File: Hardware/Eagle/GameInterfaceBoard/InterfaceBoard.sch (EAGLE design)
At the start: 22 parts

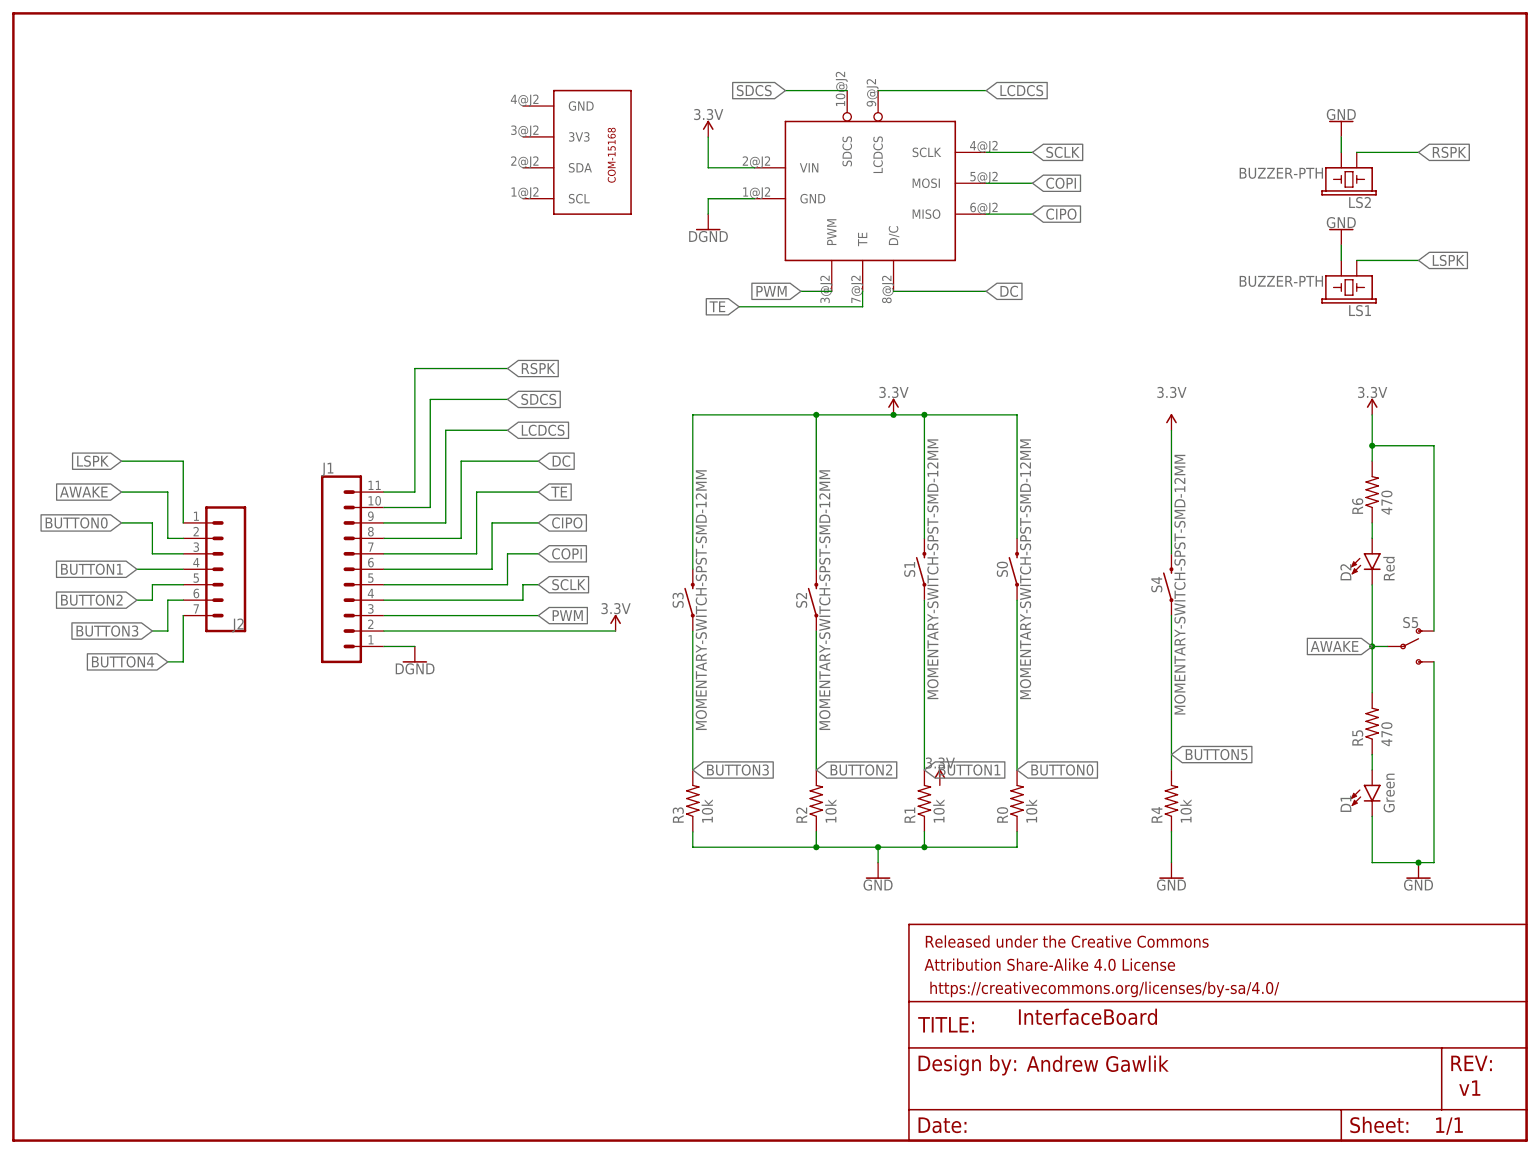
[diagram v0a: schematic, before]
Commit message: Added connection for button 4 and updated buttons to use through hole version and switched pins for easier connection on issue #2
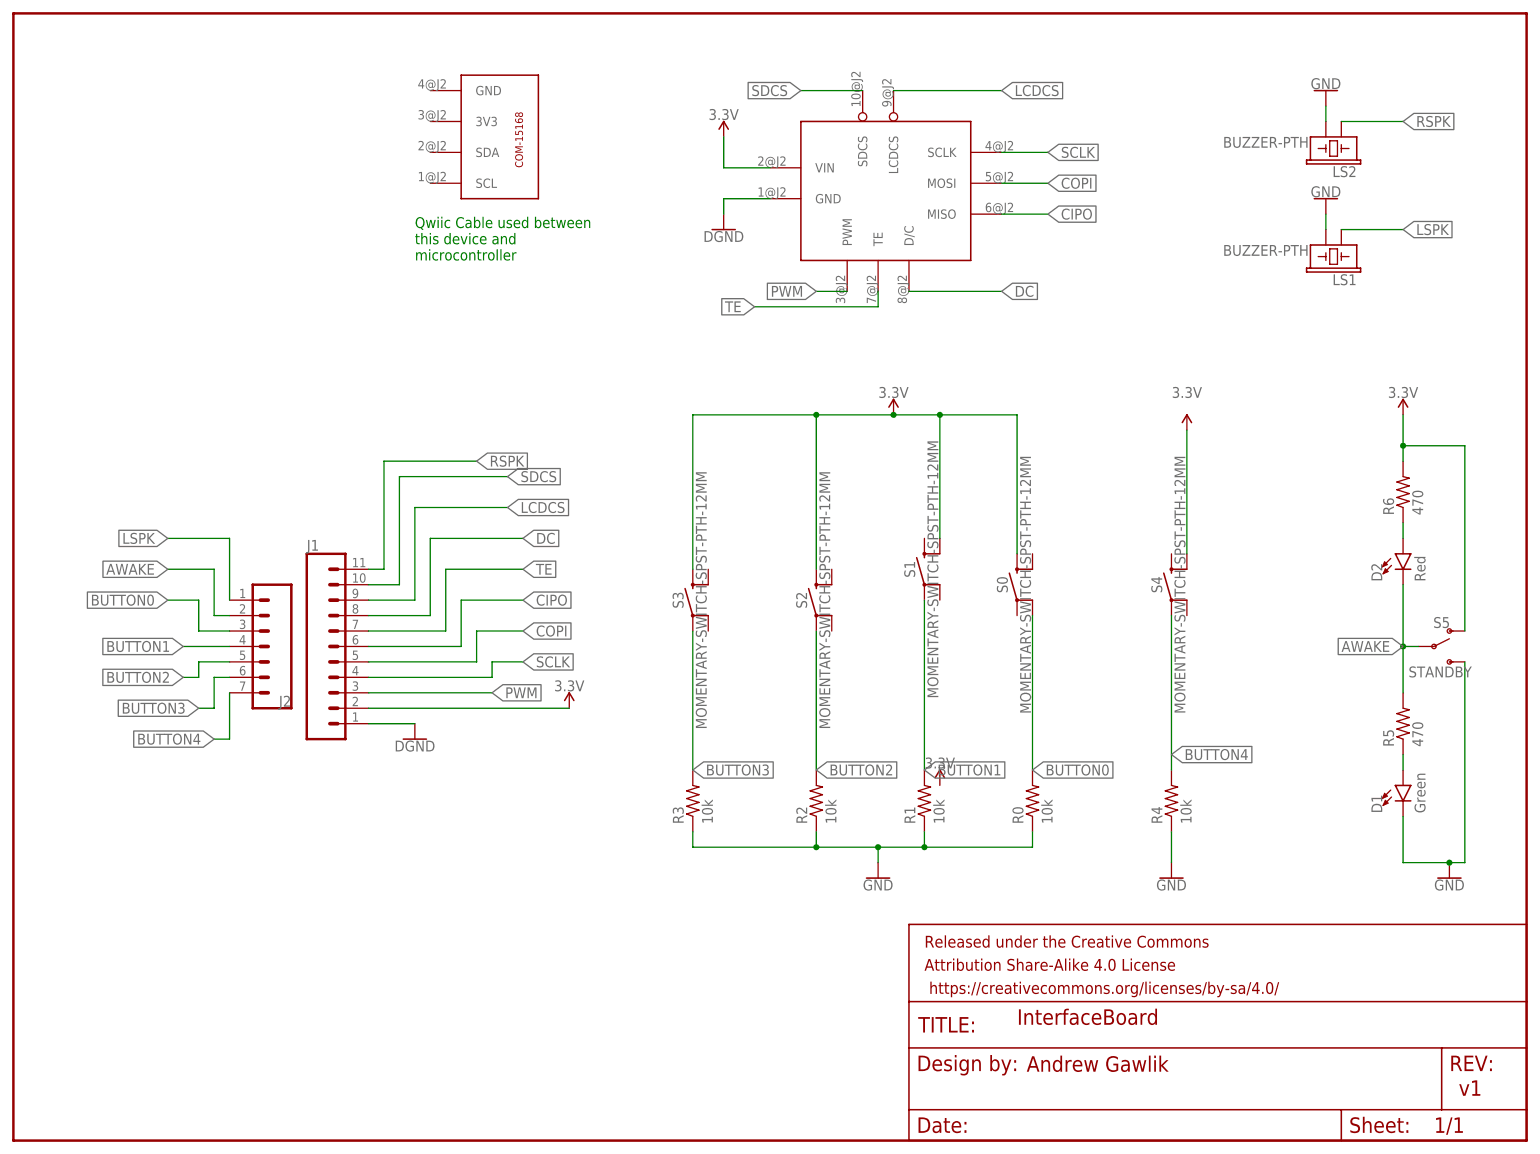
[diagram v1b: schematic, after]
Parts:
- removed A1: (no value), SparkFunBreakouts:LCD-15143
- removed U$1: COM-15168, SparkFunBreakouts:COM-15168
- added A2: TFT, SparkFunBreakouts:LCD-15143
- added A3: COM-15168, SparkFunBreakouts:COM-15168
- S0, S1, S2, S3, S4: value MOMENTARY-SWITCH-SPST-SMD-12MM -> MOMENTARY-SWITCH-SPST-PTH-12MM; device SparkFun-Switches:MOMENTARY-SWITCH-SPST-SMD-12MM -> SparkFun-Switches:MOMENTARY-SWITCH-SPST-PTH-12MM
- S5: value (none) -> STANDBY
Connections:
- removed net BUTTON5: R4.2, S4.1
- net 3.3V: now also A2.VIN, S0.3, S1.4, S2.3, S3.3, S4.4; no longer A1.VIN, S0.2, S1.2, S2.2, S3.2, S4.2
- net BUTTON0: now also S0.2; no longer S0.1
- net BUTTON4: now also R4.2, S4.1
- net CIPO: now also A2.MISO; no longer A1.MISO
- net COPI: now also A2.MOSI; no longer A1.MOSI
- net DC: now also A2.D/C; no longer A1.D/C
- net GND: now also A2.GND; no longer A1.GND
- net LCDCS: now also A2.LCDCS; no longer A1.LCDCS
- net PWM: now also A2.PWM; no longer A1.PWM
- net SCLK: now also A2.SCLK; no longer A1.SCLK
- net SDCS: now also A2.SDCS; no longer A1.SDCS
- net TE: now also A2.TE; no longer A1.TE
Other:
- note added: "Qwiic Cable used between this device and microcontroller"
- moved on the sheet: D1, D2, J1, J2, LS1, LS2, R0, R5, R6, S5
